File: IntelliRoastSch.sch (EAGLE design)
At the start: 49 parts, among them IC1 MAX31855, IC2 LP298XS, IC3 MAX31855, IC4 LP298XS, IC5 MAX31855, IC6 LP298XS, J1 1X2-3.5MM, J2 1X2-3.5MM, J3 1X2-3.5MM, U1 STM32F2XXZXT, U2 MOUDLE-BLUETOOTH-HC-05(34P-27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

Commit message: updated with headers
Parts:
- removed U1: STM32F2XXZXT, stm32f207zg:STM32F2XXZXT
- added JP4: (no value), pinhead:PINHD-2X8
- added JP5: (no value), pinhead:PINHD-2X15
- added JP6: (no value), pinhead:PINHD-2X10
- added JP7: (no value), pinhead:PINHD-2X17
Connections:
- removed net LD1: U1A.PB0
- removed net LD2(BLUE): U1B.PB7
- removed net LD3(RED): U1B.PB14
- removed net MCO: U1A.PH0/OSC_IN
- removed net RCC_OSC32_IN: U1A.PC14/OSC32_IN
- removed net RCC_OSC32_OUT: U1A.PC15-OSC32_OUT
- removed net RCC_OSC_OUT: U1A.PH1/OSC_OUT
- removed net STLK_RX: U1B.PD8
- removed net STLK_TX: U1B.PD9
- removed net TCK: U1B.PA14
- removed net TMS: U1B.PA13
- removed net USB_OVERCURRENT: U1B.PG7
- removed net USB_POWERSWITCHON: U1B.PG6
- removed net USER_BTN(B1): U1A.PC13
- new net N$100: JP7.23
- new net N$101: JP7.25
- new net N$102: JP7.27
- new net N$104: JP7.31
- new net N$105: JP7.33
- new net N$106: JP7.34
- new net N$107: JP7.32
- new net N$108: JP7.30
- new net N$109: JP7.28
- new net N$110: JP7.26
- new net N$111: JP7.24
- new net N$112: JP7.22
- new net N$113: JP7.20
- new net N$114: JP7.18
- new net N$115: JP7.16
- new net N$116: JP7.14
- new net N$117: JP7.12
- new net N$118: JP7.10
- new net N$19: JP4.1
- new net N$20: JP4.3
- new net N$25: JP4.5
- new net N$26: JP4.7
- new net N$27: JP4.9
- new net N$28: JP4.11
- new net N$29: JP4.13
- new net N$30: JP4.15
- new net N$31: JP4.16
- new net N$32: JP4.14
- new net N$33: JP4.12
- new net N$34: JP4.10
- new net N$35: JP4.8
- new net N$36: JP4.6
- new net N$37: JP4.4
- new net N$38: JP4.2
- new net N$40: JP5.3
- new net N$41: JP5.5
- new net N$42: JP5.7
- new net N$43: JP5.9
- new net N$44: JP5.11
- new net N$45: JP5.13
- new net N$46: JP5.15
- new net N$47: JP5.17
- new net N$48: JP5.19
- new net N$49: JP5.21
- new net N$50: JP5.23
- new net N$51: JP5.25
- new net N$52: JP5.27
- new net N$53: JP5.29
- new net N$54: JP5.30
- new net N$55: JP5.28
- new net N$56: JP5.26
- new net N$57: JP5.24
- new net N$58: JP5.22
- new net N$59: JP5.20
- new net N$60: JP5.18
- new net N$61: JP5.16
- new net N$62: JP5.14
- new net N$63: JP5.12
- new net N$64: JP5.10
- new net N$65: JP5.8
- new net N$67: JP5.4
- new net N$68: JP5.2
- new net N$70: JP6.3
- new net N$71: JP6.5
- new net N$72: JP6.7
- new net N$73: JP6.9
- new net N$74: JP6.11
- new net N$76: JP6.15
- new net N$77: JP6.17
- new net N$78: JP6.19
- new net N$79: JP6.2
- new net N$80: JP6.4
- new net N$81: JP6.6
- new net N$82: JP6.8
- new net N$85: JP6.14
- new net N$86: JP6.16
- new net N$87: JP6.18
- new net N$88: JP6.20
- new net N$89: JP7.1
- new net N$90: JP7.3
- new net N$91: JP7.5
- new net N$92: JP7.7
- new net N$93: JP7.9
- new net N$94: JP7.11
- new net N$95: JP7.13
- new net N$96: JP7.15
- new net N$97: JP7.17
- new net N$98: JP7.19
- net BT_RX: now also JP5.1; no longer U1A.PA3
- net BT_TX: now also JP5.6; no longer U1B.PD5
- net SPI1_CS2: now also JP7.8; no longer U1A.PF14
- net SPI1_CS3: now also JP7.6; no longer U1A.PE11
- net SPI1_MISO: now also JP6.12; no longer U1A.PA6
- net SPI1_MOSI: now also JP6.13; no longer U1B.PB5
- net SPI1_SCK: now also JP6.10; no longer U1A.PA5
- net SPI2_CS0: now also JP7.2; no longer U1A.PF13
- net SPI2_CS1: now also JP7.4; no longer U1A.PE9
- net TIM2_CH1: now also JP7.29; no longer U1A.PA0-WKUP
- net TIM3_CH1: now also JP6.1; no longer U1B.PC6
- net TIM4_CH1: now also JP7.21; no longer U1B.PD12

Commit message: moved componenets into separate pages for each subsystem
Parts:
- removed C1, C2, C4, C5, C7, C8: 10uF, adafruit:C-USC0805K
- removed C3, C6, C9: 0.01µF, microbuilder:CAP_CERAMIC_0805
- removed D1, D3, D5: 1n4148, adafruit:DIODESOD-323F
- removed D2, D4, D6: 1N4148, adafruit:DIODESOD-323F
- removed FB1, FB2, FB3, FB4, FB5, FB6: Ferrite, microbuilder:FERRITE_0805
- removed IC1, IC3, IC5: MAX31855, adafruit:MAX6675
- removed IC2, IC4, IC6: LP298XS, adafruit:LP298XS
- removed J1, J2, J3: 1X2-3.5MM, adafruit:1X2-3.5MM
- removed JP1, JP2, JP3: Breakout, microbuilder:HEADER-1X676MIL
- removed R1, R2, R3, R4, R5, R6: 10K, adafruit:R-US_R0805
- added C15, C16, C18, C19, C21, C22: 10uF, adafruit:C-USC0805K
- added C17, C20, C23: 0.01µF, microbuilder:CAP_CERAMIC_0805
- added D10, D12, D8: 1N4148, adafruit:DIODESOD-323F
- added D11, D7, D9: 1n4148, adafruit:DIODESOD-323F
- added FB10, FB11, FB12, FB7, FB8, FB9: Ferrite, microbuilder:FERRITE_0805
- added IC10, IC12, IC8: LP298XS, adafruit:LP298XS
- added IC11, IC7, IC9: MAX31855, adafruit:MAX6675
- added J4, J5, J6: 1X2-3.5MM, adafruit:1X2-3.5MM
- added JP10, JP8, JP9: Breakout, microbuilder:HEADER-1X676MIL
- added R10, R11, R12, R13, R14, R9: 10K, adafruit:R-US_R0805
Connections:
- removed net CS: D2.A, IC1./CS, R2.2
- removed net CS1: D4.A, IC3./CS, R4.2
- removed net CS2: D6.A, IC5./CS, R6.2
- removed net DO: IC1.DO, JP1.4
- removed net DO1: IC3.DO, JP2.4
- removed net DO2: IC5.DO, JP3.4
- removed net N$1: FB1.P$1, J1.2
- removed net N$10: C6.P$1, FB3.P$2, IC3.T-
- removed net N$11: FB4.P$1, J2.1
- removed net N$12: C6.P$2, FB4.P$2, IC3.T+
- removed net N$13: D6.C, JP3.5
- removed net N$14: D5.C, JP3.6
- removed net N$15: FB5.P$1, J3.2
- removed net N$16: C9.P$1, FB5.P$2, IC5.T-
- removed net N$17: FB6.P$1, J3.1
- removed net N$18: C9.P$2, FB6.P$2, IC5.T+
- removed net N$2: D2.C, JP1.5
- removed net N$3: D1.C, JP1.6
- removed net N$4: C3.P$1, FB1.P$2, IC1.T-
- removed net N$5: FB2.P$1, J1.1
- removed net N$6: C3.P$2, FB2.P$2, IC1.T+
- removed net N$7: D4.C, JP2.5
- removed net N$8: D3.C, JP2.6
- removed net N$9: FB3.P$1, J2.2
- removed net SCK: D1.A, IC1.SCK, R1.2
- removed net SCK1: D3.A, IC3.SCK, R3.2
- removed net SCK2: D5.A, IC5.SCK, R5.2
- new net CS3: D8.A, IC7./CS, R10.2
- new net CS4: D10.A, IC9./CS, R12.2
- new net CS5: D12.A, IC11./CS, R14.2
- new net DO3: IC7.DO, JP8.4
- new net DO4: IC9.DO, JP9.4
- new net DO5: IC11.DO, JP10.4
- new net N$103: D9.C, JP9.6
- new net N$119: FB9.P$1, J5.2
- new net N$120: C20.P$1, FB9.P$2, IC9.T-
- new net N$121: FB10.P$1, J5.1
- new net N$122: C20.P$2, FB10.P$2, IC9.T+
- new net N$123: D12.C, JP10.5
- new net N$124: D11.C, JP10.6
- new net N$125: FB11.P$1, J6.2
- new net N$126: C23.P$1, FB11.P$2, IC11.T-
- new net N$127: FB12.P$1, J6.1
- new net N$128: C23.P$2, FB12.P$2, IC11.T+
- new net N$39: D8.C, JP8.5
- new net N$66: D7.C, JP8.6
- new net N$69: FB7.P$1, J4.2
- new net N$75: C17.P$1, FB7.P$2, IC7.T-
- new net N$83: FB8.P$1, J4.1
- new net N$84: C17.P$2, FB8.P$2, IC7.T+
- new net N$99: D10.C, JP9.5
- new net SCK3: D7.A, IC7.SCK, R9.2
- new net SCK4: D9.A, IC9.SCK, R11.2
- new net SCK5: D11.A, IC11.SCK, R13.2
- net +3V3: now also C15.1, C16.1, C18.1, C19.1, C21.1, C22.1, IC10.VOUT, IC11.VCC, IC12.VOUT, IC7.VCC, IC8.VOUT, IC9.VCC, JP10.2, JP8.2, JP9.2, R10.1, R11.1, R12.1, R13.1, R14.1, R9.1; no longer C1.1, C2.1, C4.1, C5.1, C7.1, C8.1, IC1.VCC, IC2.VOUT, IC3.VCC, IC4.VOUT, IC5.VCC, IC6.VOUT, JP1.2, JP2.2, JP3.2, R1.1, R2.1, R3.1, R4.1, R5.1, R6.1
- net +5V: now also IC10.EN, IC10.VIN, IC12.EN, IC12.VIN, IC8.EN, IC8.VIN, JP10.1, JP8.1, JP9.1; no longer IC2.EN, IC2.VIN, IC4.EN, IC4.VIN, IC6.EN, IC6.VIN, JP1.1, JP2.1, JP3.1
- net GND: now also C15.2, C16.2, C18.2, C19.2, C21.2, C22.2, IC10.GND, IC11.GND, IC12.GND, IC7.GND, IC8.GND, IC9.GND, JP10.3, JP8.3, JP9.3; no longer C1.2, C2.2, C4.2, C5.2, C7.2, C8.2, IC1.GND, IC2.GND, IC3.GND, IC4.GND, IC5.GND, IC6.GND, JP1.3, JP2.3, JP3.3

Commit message: Added page for 3v3 Power Regulator
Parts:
- added C1: (no value), adafruit:C-USC1210
- added C2: (no value), adafruit:C-USC0805
- added C3, C4: (no value), adafruit:C-USC0603
- added D1: (no value), eagle-ltspice:SCHOTTKY-DIODESMC
- added L1: LPOWER_REGULATOR, IntelliRoast:LPOWER_REGULATOR
- added U1: LM2576HVS-3.3/NOPB, LM2576HVS-3.3_NOPB:LM2576HVS-3.3/NOPB
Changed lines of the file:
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@@
 <layer number="54" name="bGND_GNDA" color="1" fill="9" visible="no" active="no"/>
 <layer number="56" name="wert" color="7" fill="1" visible="no" active="no"/>
+<layer number="57" name="tCAD" color="7" fill="1" visible="no" active="no"/>
+<layer number="59" name="tCarbon" color="7" fill="1" visible="no" active="no"/>
+<layer number="60" name="bCarbon" color="7" fill="1" visible="no" active="no"/>
 <layer number="88" name="SimResults" color="9" fill="1" visible="no" active="yes"/>
 <layer number="89" name="SimProbes" color="9" fill="1" visible="yes" active="yes"/>
@@
 <layer number="111" name="LPC17xx" color="7" fill="1" visible="yes" active="yes"/>
 <layer number="112" name="tSilk" color="7" fill="1" visible="yes" active="yes"/>
+<layer number="113" name="ReferenceLS" color="7" fill="1" visible="no" active="no"/>
+<layer number="114" name="Badge_Outline" color="7" fill="1" visible="no" active="no"/>
+<layer number="115" name="ReferenceISLANDS" color="7" fill="1" visible="no" active="no"/>
 <layer number="116" name="Patch_BOT" color="9" fill="4" visible="yes" active="yes"/>
+<layer number="118" name="Rect_Pads" color="7" fill="1" visible="no" active="no"/>
 <layer number="121" name="_tsilk" color="7" fill="1" visible="yes" active="yes"/>
 <layer number="122" name="_bsilk" color="7" fill="1" visible="yes" active="yes"/>
@@
 <layer number="127" name="_tValues" color="7" fill="1" visible="yes" active="yes"/>
 <layer number="128" name="_bValues" color="7" fill="1" visible="yes" active="yes"/>
+<layer number="129" name="Mask" color="7" fill="1" visible="yes" active="yes"/>
 <layer number="131" name="tAdjust" color="7" fill="1" visible="no" active="yes"/>
 <layer number="132" name="bAdjust" color="7" fill="1" visible="no" active="yes"/>
 <layer number="144" name="Drill_legend" color="7" fill="1" visible="yes" active="yes"/>
+<layer number="150" name="Notes" color="7" fill="1" visible="no" active="yes"/>
 <layer number="151" name="HeatSink" color="7" fill="1" visible="yes" active="yes"/>
 <layer number="152" name="_bDocu" color="7" fill="1" visible="yes" active="yes"/>
+<layer number="153" name="FabDoc1" color="6" fill="1" visible="no" active="no"/>
+<layer number="154" name="FabDoc2" color="2" fill="1" visible="no" active="no"/>
+<layer number="155" name="FabDoc3" color="7" fill="15" visible="no" active="no"/>
 <layer number="199" name="Contour" color="7" fill="1" visible="yes" active="yes"/>
 <layer number="200" name="200bmp" color="1" fill="10" visible="no" active="no"/>
@@
 <layer number="223" name="223bmp" color="24" fill="1" visible="no" active="no"/>
 <layer number="224" name="224bmp" color="25" fill="1" visible="no" active="no"/>
+<layer number="225" name="225bmp" color="7" fill="1" visible="yes" active="yes"/>
+<layer number="226" name="226bmp" color="7" fill="1" visible="yes" active="yes"/>
+<layer number="227" name="227bmp" color="7" fill="1" visible="yes" active="yes"/>
+<layer number="228" name="228bmp" color="7" fill="1" visible="yes" active="yes"/>
+<layer number="229" name="229bmp" color="7" fill="1" visible="yes" active="yes"/>
+<layer number="230" name="230bmp" color="7" fill="1" visible="yes" active="yes"/>
+<layer number="231" name="Eagle3D_PG1" color="7" fill="1" visible="no" active="no"/>
+<layer number="232" name="Eagle3D_PG2" color="7" fill="1" visible="no" active="no"/>
+<layer number="233" name="Eagle3D_PG3" color="7" fill="1" visible="no" active="no"/>
 <layer number="248" name="Housing" color="7" fill="1" visible="yes" active="yes"/>
 <layer number="249" name="Edge" color="7" fill="1" visible="yes" active="yes"/>
@@
 <layer number="251" name="SMDround" color="12" fill="11" visible="no" active="no"/>
 <layer number="254" name="cooling" color="7" fill="1" visible="yes" active="yes"/>
+<layer number="255" name="routoute" color="7" fill="1" visible="yes" active="yes"/>
 </layers>
 <schematic xreflabel="%F%N/%S.%C%R" xrefpart="/%S.%C%R">
@@
 <part name="JP6" library="pinhead" library_urn="urn:adsk.eagle:library:325" deviceset="PINHD-2X10" device="" package3d_urn="urn:adsk.eagle:package:22405/2"/>
 <part name="JP7" library="pinhead" library_urn="urn:adsk.eagle:library:325" deviceset="PINHD-2X17" device="" package3d_urn="urn:adsk.eagle:package:22495/2"/>
+<part name="U1" library="LM2576HVS-3.3_NOPB" deviceset="LM2576HVS-3.3/NOPB" device=""/>
+<part name="D1" library="eagle-ltspice" library_urn="urn:adsk.eagle:library:217" deviceset="SCHOTTKY-DIODE" device="SMC" package3d_urn="urn:adsk.eagle:package:13317/1"/>
+<part name="C1" library="adafruit" library_urn="urn:adsk.eagle:library:420" deviceset="C-US" device="C1210" package3d_urn="urn:adsk.eagle:package:6240334/1"/>
+<part name="C2" library="adafruit" library_urn="urn:adsk.eagle:library:420" deviceset="C-US" device="C0805" package3d_urn="urn:adsk.eagle:package:6240337/1"/>
+<part name="C3" library="adafruit" library_urn="urn:adsk.eagle:library:420" deviceset="C-US" device="C0603" package3d_urn="urn:adsk.eagle:package:6240338/1"/>
+<part name="C4" library="adafruit" library_urn="urn:adsk.eagle:library:420" deviceset="C-US" device="C0603" package3d_urn="urn:adsk.eagle:package:6240338/1"/>
+<part name="L1" library="IntelliRoast" deviceset="L" device="POWER_REGULATOR"/>
 </parts>
 <sheets>
@@
 </plain>
 <instances>
+<instance part="U1" gate="G$1" x="55.88" y="53.34" smashed="yes">
+<attribute name="NAME" x="45.6713" y="64.5593" size="1.78653125" layer="95"/>
+<attribute name="VALUE" x="45.7031" y="40.6229" size="1.78093125" layer="96"/>
+</instance>
+<instance part="D1" gate="G$1" x="83.82" y="25.4" smashed="yes">
+<attribute name="NAME" x="81.915" y="23.114" size="1.778" layer="95" rot="R90"/>
+<attribute name="VALUE" x="87.249" y="23.114" size="1.778" layer="96" rot="R90"/>
+</instance>
+<instance part="C1" gate="G$1" x="104.14" y="43.18" smashed="yes">
+<attribute name="NAME" x="105.156" y="43.815" size="1.778" layer="95"/>
+<attribute name="VALUE" x="105.156" y="38.989" size="1.778" layer="96"/>
+</instance>
+<instance part="C2" gate="G$1" x="116.84" y="43.18" smashed="yes">
+<attribute name="NAME" x="117.856" y="43.815" size="1.778" layer="95"/>
+<attribute name="VALUE" x="117.856" y="38.989" size="1.778" layer="96"/>
+</instance>
+<instance part="C3" gate="G$1" x="127" y="43.18" smashed="yes">
+<attribute name="NAME" x="128.016" y="43.815" size="1.778" layer="95"/>
+<attribute name="VALUE" x="128.016" y="38.989" size="1.778" layer="96"/>
+</instance>
+<instance part="C4" gate="G$1" x="137.16" y="43.18" smashed="yes">
+<attribute name="NAME" x="138.176" y="43.815" size="1.778" layer="95"/>
+<attribute name="VALUE" x="138.176" y="38.989" size="1.778" layer="96"/>
+</instance>
+<instance part="L1" gate="G$1" x="53.34" y="22.86" smashed="yes" rot="R90">
+<attribute name="NAME" x="58.42" y="21.59" size="1.778" layer="95" rot="R180"/>
+<attribute name="VALUE" x="58.42" y="26.67" size="1.778" layer="96" rot="R180"/>
+</instance>
 </instances>
 <busses>

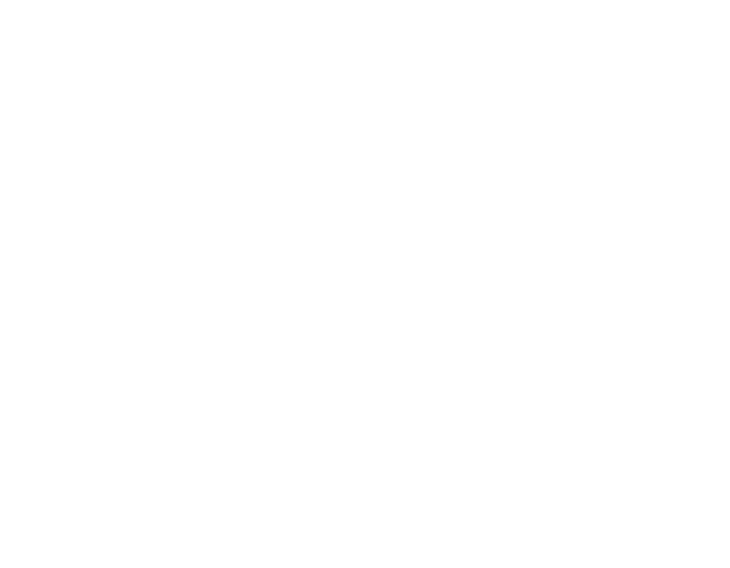
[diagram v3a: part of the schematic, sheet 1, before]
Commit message: fan driver added
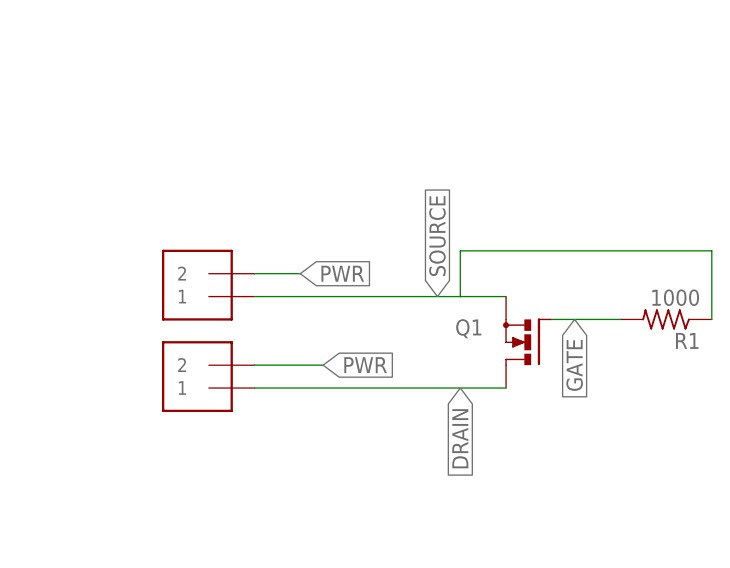
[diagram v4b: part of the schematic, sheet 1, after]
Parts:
- added J1, J2: 1X2-3.5MM, adafruit:1X2-3.5MM
- added Q1: (no value), transistor-power:PMOSFET_NTO220BH
- added R1: 1000, rcl:R-US_R0603
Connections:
- new net DRAIN: J1.1, Q1.D
- new net GATE: Q1.G, R1.2
- new net PWR: J1.2, J2.2
- new net SOURCE: J2.1, Q1.S, R1.1

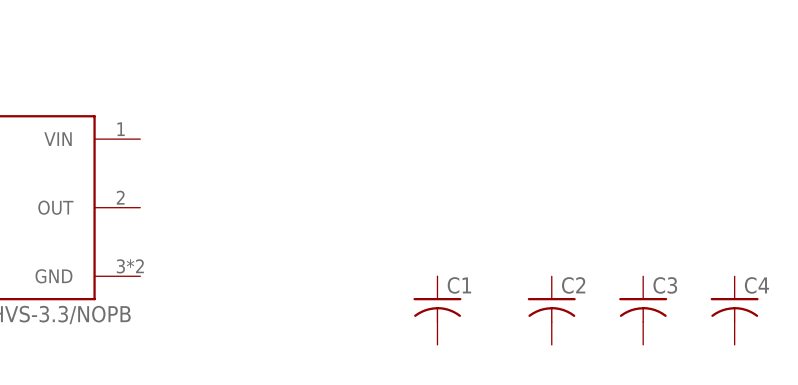
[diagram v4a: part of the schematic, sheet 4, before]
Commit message: Merged changes to have both power regulation and fan controller
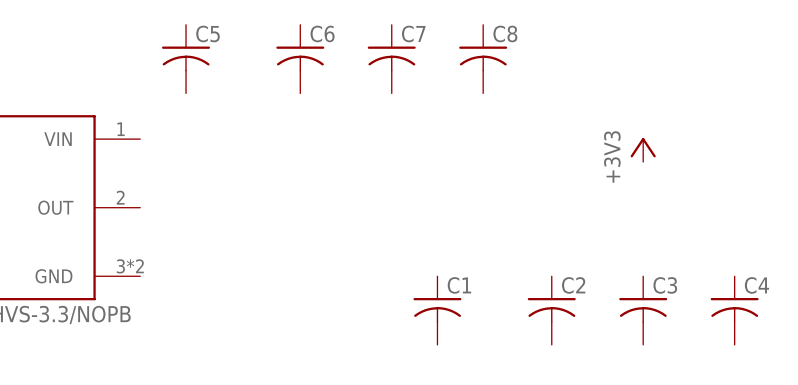
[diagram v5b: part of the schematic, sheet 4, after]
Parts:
- added C5: (no value), adafruit:C-USC1210
- added C6: (no value), adafruit:C-USC0805
- added C7, C8: (no value), adafruit:C-USC0603
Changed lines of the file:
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@@
 <part name="J1" library="adafruit" deviceset="1X2" device="-3.5MM"/>
 <part name="J2" library="adafruit" deviceset="1X2" device="-3.5MM"/>
+<part name="+3V1" library="supply1" library_urn="urn:adsk.eagle:library:371" deviceset="+3V3" device=""/>
+<part name="C5" library="adafruit" library_urn="urn:adsk.eagle:library:420" deviceset="C-US" device="C1210" package3d_urn="urn:adsk.eagle:package:6240334/1"/>
+<part name="C6" library="adafruit" library_urn="urn:adsk.eagle:library:420" deviceset="C-US" device="C0805" package3d_urn="urn:adsk.eagle:package:6240337/1"/>
+<part name="C7" library="adafruit" library_urn="urn:adsk.eagle:library:420" deviceset="C-US" device="C0603" package3d_urn="urn:adsk.eagle:package:6240338/1"/>
+<part name="C8" library="adafruit" library_urn="urn:adsk.eagle:library:420" deviceset="C-US" device="C0603" package3d_urn="urn:adsk.eagle:package:6240338/1"/>
 </parts>
 <sheets>
@@
 <attribute name="VALUE" x="58.42" y="26.67" size="1.778" layer="96" rot="R180"/>
 </instance>
+<instance part="+3V1" gate="G$1" x="127" y="60.96" smashed="yes">
+<attribute name="VALUE" x="124.46" y="55.88" size="1.778" layer="96" rot="R90"/>
+</instance>
+<instance part="C5" gate="G$1" x="76.2" y="71.12" smashed="yes">
+<attribute name="NAME" x="77.216" y="71.755" size="1.778" layer="95"/>
+<attribute name="VALUE" x="77.216" y="66.929" size="1.778" layer="96"/>
+</instance>
+<instance part="C6" gate="G$1" x="88.9" y="71.12" smashed="yes">
+<attribute name="NAME" x="89.916" y="71.755" size="1.778" layer="95"/>
+<attribute name="VALUE" x="89.916" y="66.929" size="1.778" layer="96"/>
+</instance>
+<instance part="C7" gate="G$1" x="99.06" y="71.12" smashed="yes">
+<attribute name="NAME" x="100.076" y="71.755" size="1.778" layer="95"/>
+<attribute name="VALUE" x="100.076" y="66.929" size="1.778" layer="96"/>
+</instance>
+<instance part="C8" gate="G$1" x="109.22" y="71.12" smashed="yes">
+<attribute name="NAME" x="110.236" y="71.755" size="1.778" layer="95"/>
+<attribute name="VALUE" x="110.236" y="66.929" size="1.778" layer="96"/>
+</instance>
 </instances>

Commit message: Moved Fan controller to separate page, reworked it a bit, and Added todo's to some pages
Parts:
- removed IC10, IC12, IC8: LP298XS, adafruit:LP298XS
- added D2: (no value), adafruit:DIODESMA
- added J3, J7: 1X2-3.5MM, adafruit:1X2-3.5MM
- added Q2: (no value), transistor-power:PMOSFET_NTO220BH
- added R2: 1000, rcl:R-US_R0603
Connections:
- new net +12V: C5.1, C6.1, C7.1, C8.1, D2.C, J3.2, J7.2, U1.VIN
- new net N$1: D1.A, L1.1, U1.OUT
- new net N$2: D2.A, J7.1, Q2.D
- new net N$3: Q2.G, R2.2
- net +3V3: now also C1.1, C2.1, C3.1, C4.1, L1.2, U1.FB; no longer IC10.VOUT, IC12.VOUT, IC8.VOUT
- net +5V: no longer IC10.EN, IC10.VIN, IC12.EN, IC12.VIN, IC8.EN, IC8.VIN
- net GND: now also C1.2, C2.2, C3.2, C4.2, C5.2, C6.2, C7.2, C8.2, D1.C, J3.1, Q2.S, R2.1, U1.!ON!/OFF, U1.GND; no longer IC10.GND, IC12.GND, IC8.GND
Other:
- note added: "+ Fan -"
- note added: "+12V In"
- note added: "12V -> 3V3 Regulator"
- note added: "TODO: - Add parts to BOM"
- note added: "TODO: - Change out caps to "Adafruit" equivalent for consistancy - Double check wiring - Add a way to get into programming mode so we can change the BT Name to "IntelliRoast" -Add parts to BOM"
- note added: "TODO: -Remove Header pins and tie directly into STM32F207 Spi bus -Double check all the parts have the correct footprints -Remove any 5V rails -Add Parts to BOM"
